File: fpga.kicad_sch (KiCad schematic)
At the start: 27 parts

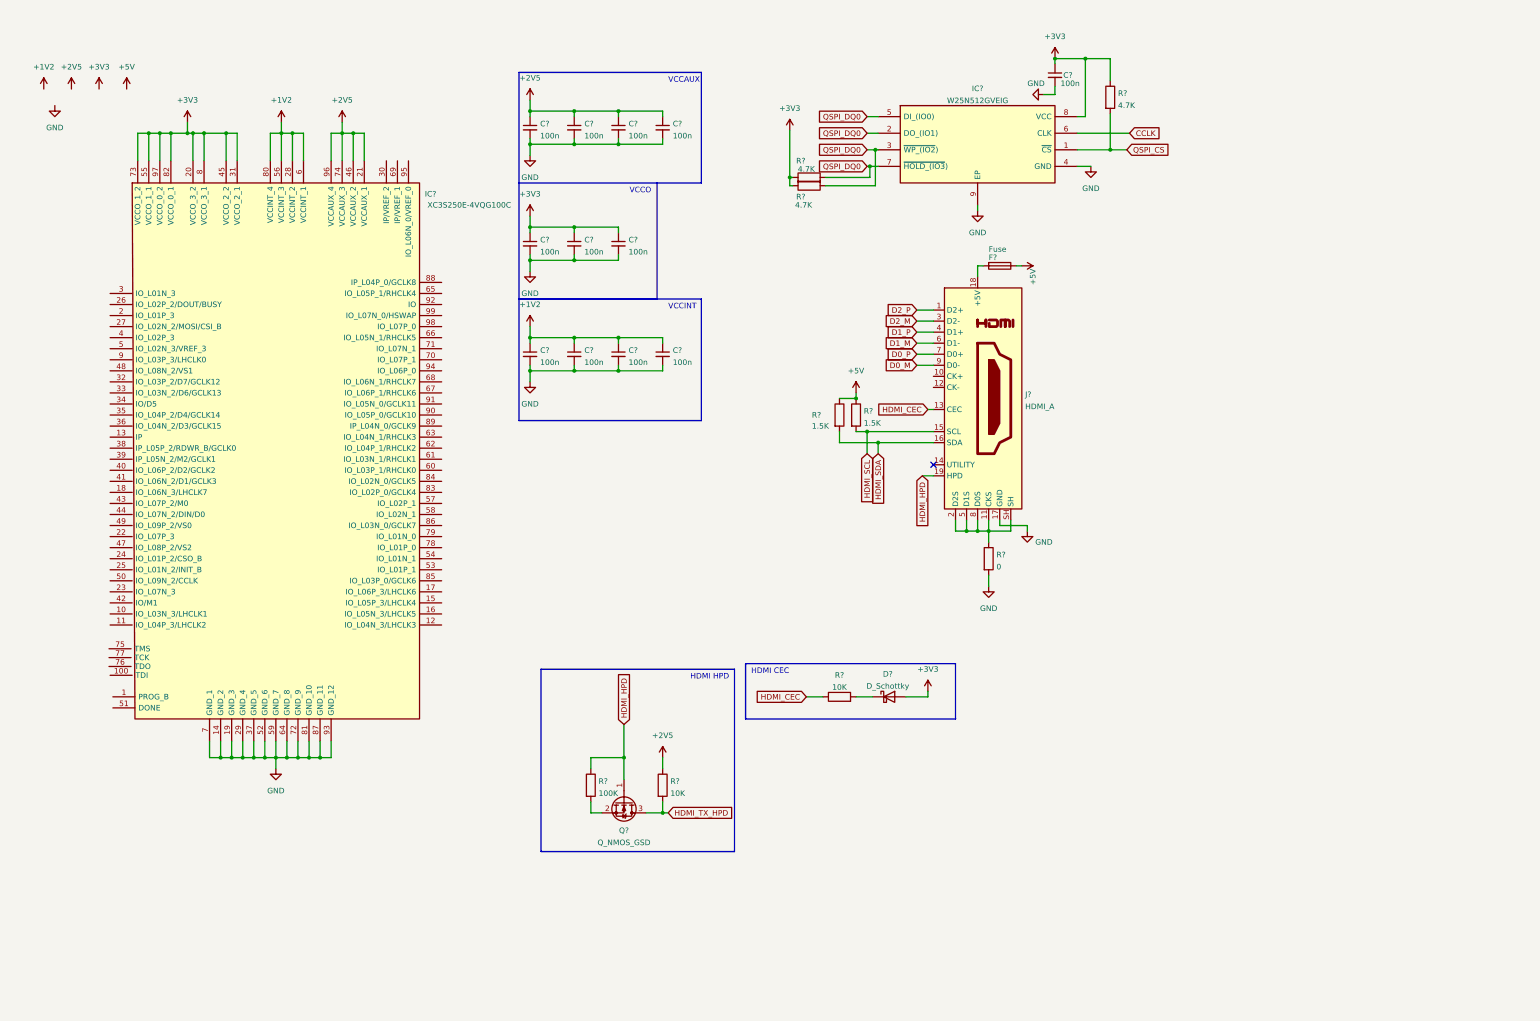
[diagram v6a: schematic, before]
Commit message: Added HDMI to FPGA
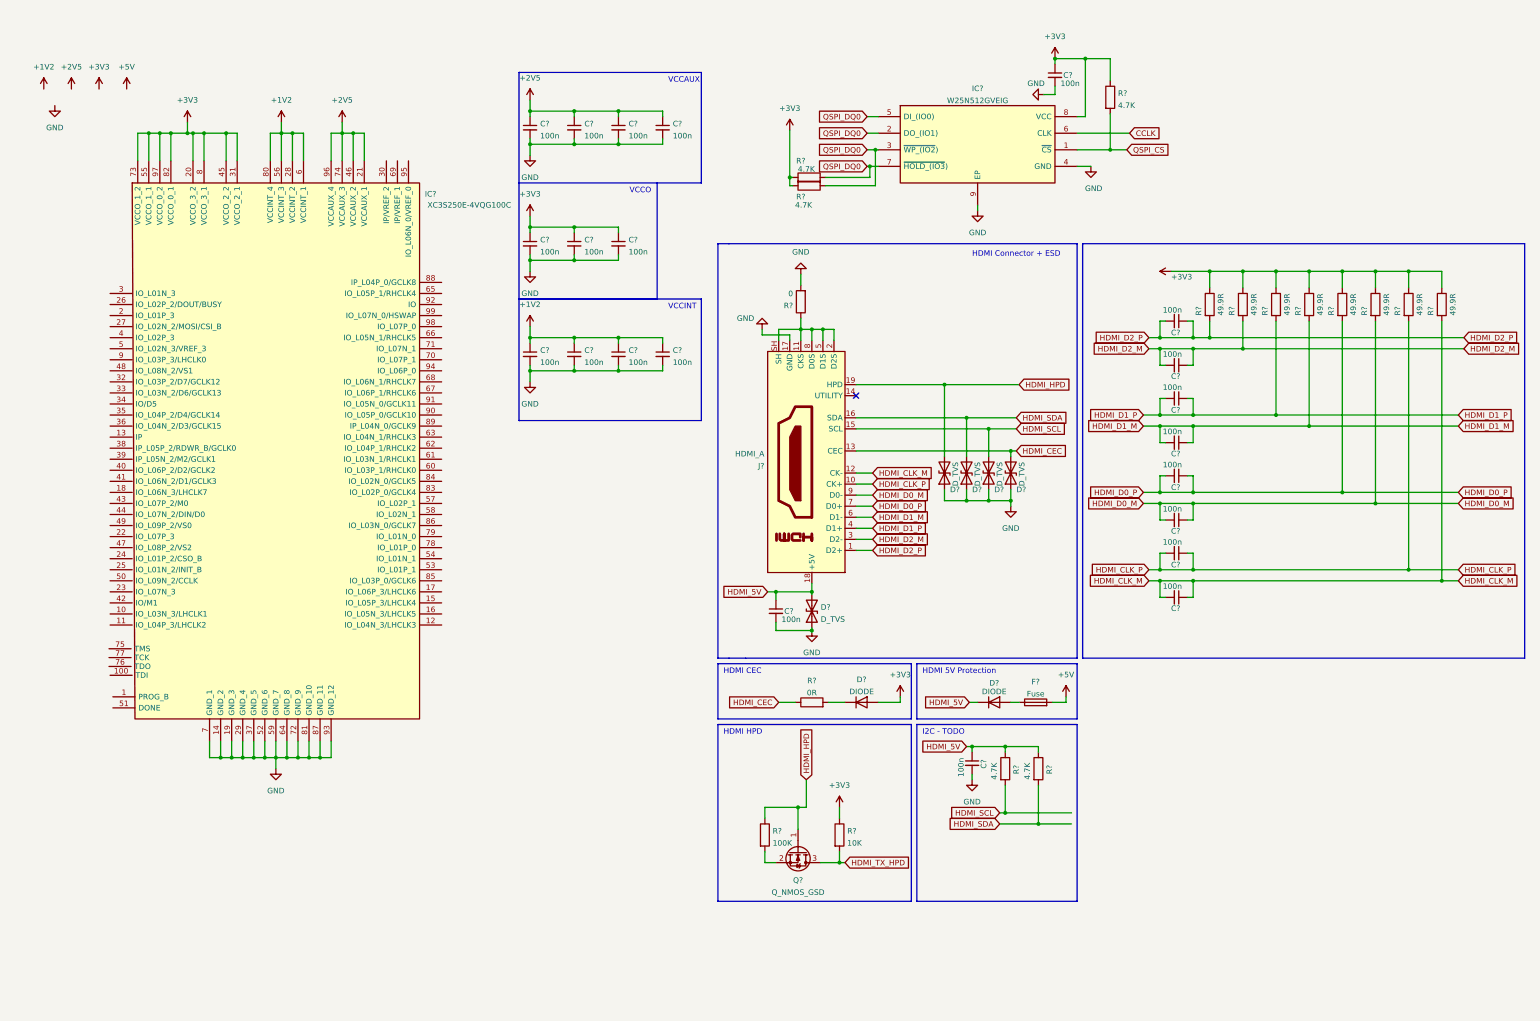
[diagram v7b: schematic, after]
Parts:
- removed D?: D_Schottky, symbol Device:D_Schottky
- removed F?: Fuse, symbol Device:Fuse
- removed R? (x2): 1.5K, symbol Device:R
- added C? (x10): 100n, symbol Device:C_Small
- added D? (x5): D_TVS, symbol Device:D_TVS
- added D? (x2): DIODE, symbol Simulation_SPICE:DIODE
- added F?: Fuse, symbol Device:Fuse
- added R? (x8): 49.9R, symbol Device:R
- added R? (x2): 4.7K, symbol Device:R
- R?: value 10K -> 0R
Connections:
- net +2V5: no longer R?.1
- net +3V3: now also R?.1, D?.1 (A), R?.1, R?.1, R?.1, R?.1, R?.1, R?.1, R?.1, R?.1
- net +5V: now also F?.2
- net GND: now also C?.2, C?.2, D?.1 (A1), D?.1 (A1), D?.1 (A1), D?.1 (A1), D?.1 (A1)
- net HDMI_CEC: now also D?.2 (A2)
- net HDMI_HPD: now also D?.2 (A2)
- net HDMI_SCL: now also D?.2 (A2), R?.2
- net HDMI_SDA: now also D?.2 (A2), R?.2
- net at R?.2: now also D?.2 (K)
- net HDMI_CLK_P: now reaches J?.10 (CK+)
- net HDMI_CLK_P: now also C?.1, C?.2, R?.2
- net HDMI_CLK_M: now reaches J?.12 (CK-)
- net HDMI_CLK_M: now also C?.1, C?.2, R?.2
- net HDMI_5V: now reaches J?.18 (+5V)
- net HDMI_5V: now also C?.1, C?.1, D?.2 (A2), D?.2 (K), R?.1, R?.1
- net D0_M renamed HDMI_D0_M
- net HDMI_D0_M: now also C?.1, C?.2, R?.2
- net D0_P renamed HDMI_D0_P
- net HDMI_D0_P: now also C?.1, C?.2, R?.2
- net D1_M renamed HDMI_D1_M
- net HDMI_D1_M: now also C?.1, C?.2, R?.2
- net D1_P renamed HDMI_D1_P
- net HDMI_D1_P: now also C?.1, C?.2, R?.2
- net D2_M renamed HDMI_D2_M
- net HDMI_D2_M: now also C?.1, C?.2, R?.2
- net D2_P renamed HDMI_D2_P
- net HDMI_D2_P: now also C?.1, C?.2, R?.2
- new net: D?.1 (A), F?.1
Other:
- note added: "HDMI 5V Protection"
- note added: "HDMI Connector + ESD"
- note added: "I2C - TODO"
- moved on the sheet: J?, Q?, R?

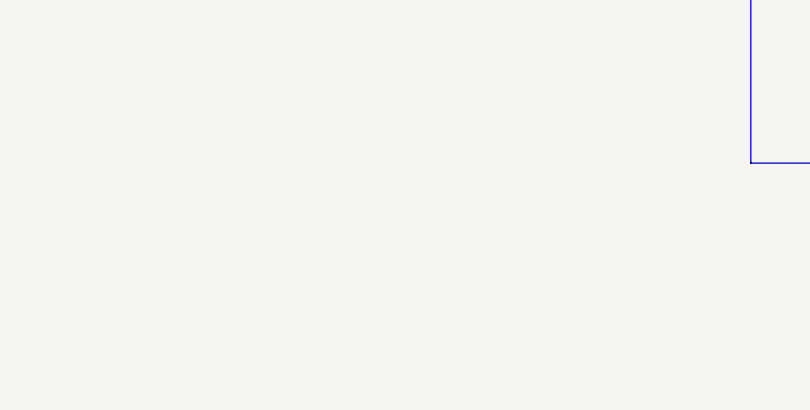
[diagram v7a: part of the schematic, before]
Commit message: added i2c level shifter ic
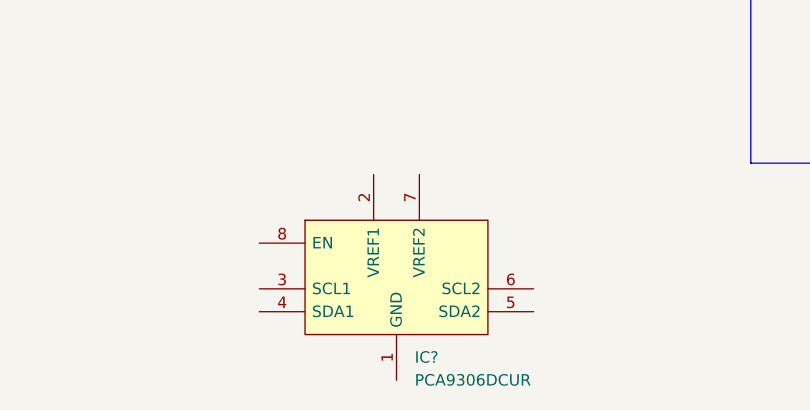
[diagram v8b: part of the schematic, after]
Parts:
- added IC?: PCA9306DCUR, SOP50P310X90-8N, symbol fpga:PCA9306DCUR
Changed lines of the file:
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@@
     (pin "99")
+  )
+  (symbol (lib_id "fpga:PCA9306DCUR") (at 121.92 220.98 0) (unit 1)
+    (in_bom yes) (on_board yes) (fields_autoplaced)
+    (property "Reference" "IC?" (id 0) (at 139.1794 233.68 0)
+      (effects (font (size 1.27 1.27)) (justify left))
+    )
+    (property "Value" "PCA9306DCUR" (id 1) (at 139.1794 236.22 0)
+      (effects (font (size 1.27 1.27)) (justify left))
+    )
+    (property "Footprint" "SOP50P310X90-8N" (id 2) (at 148.59 218.44 0)
+      (effects (font (size 1.27 1.27)) (justify left) hide)
+    )
+    (property "Datasheet" "http://www.ti.com/lit/gpn/pca9306" (id 3) (at 148.59 220.98 0)
+      (effects (font (size 1.27 1.27)) (justify left) hide)
+    )
+    (property "Description" "2-Bit Bidirectional I2C Bus and SMBus Voltage-Level Shifter" (id 4) (at 148.59 223.52 0)
+      (effects (font (size 1.27 1.27)) (justify left) hide)
+    )
+    (property "Height" "0.9" (id 5) (at 148.59 226.06 0)
+      (effects (font (size 1.27 1.27)) (justify left) hide)
+    )
+    (property "Mouser Part Number" "595-PCA9306DCUR" (id 6) (at 148.59 228.6 0)
+      (effects (font (size 1.27 1.27)) (justify left) hide)
+    )
+    (property "Mouser Price/Stock" "https://www.mouser.co.uk/ProductDetail/Texas-Instruments/PCA9306DCUR?qs=wgAEGBTxy7nQr5PRxNBUNA%3D%3D" (id 7) (at 148.59 231.14 0)
+      (effects (font (size 1.27 1.27)) (justify left) hide)
+    )
+    (property "Manufacturer_Name" "Texas Instruments" (id 8) (at 148.59 233.68 0)
+      (effects (font (size 1.27 1.27)) (justify left) hide)
+    )
+    (property "Manufacturer_Part_Number" "PCA9306DCUR" (id 9) (at 148.59 236.22 0)
+      (effects (font (size 1.27 1.27)) (justify left) hide)
+    )
+    (pin "1")
+    (pin "2")
+    (pin "3")
+    (pin "4")
+    (pin "5")
+    (pin "6")
+    (pin "7")
+    (pin "8")
   )
   (symbol (lib_id "power:+1V2") (at 76.2 33.02 0) (unit 1)
